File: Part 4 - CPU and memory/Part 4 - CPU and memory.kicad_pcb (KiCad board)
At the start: 2 copper layers, 100 x 100 mm, 50 parts, among them J1 BUS 1, U1 74AHC00, U10 SST39SF010, U11 AS6C4008, U2 74AHC32, U3 74AHC32, U4 74AHC32, U5 74HC563, U6 74AHC174, U7 74AHC138, U8 Z80C0010, U9 74HC563

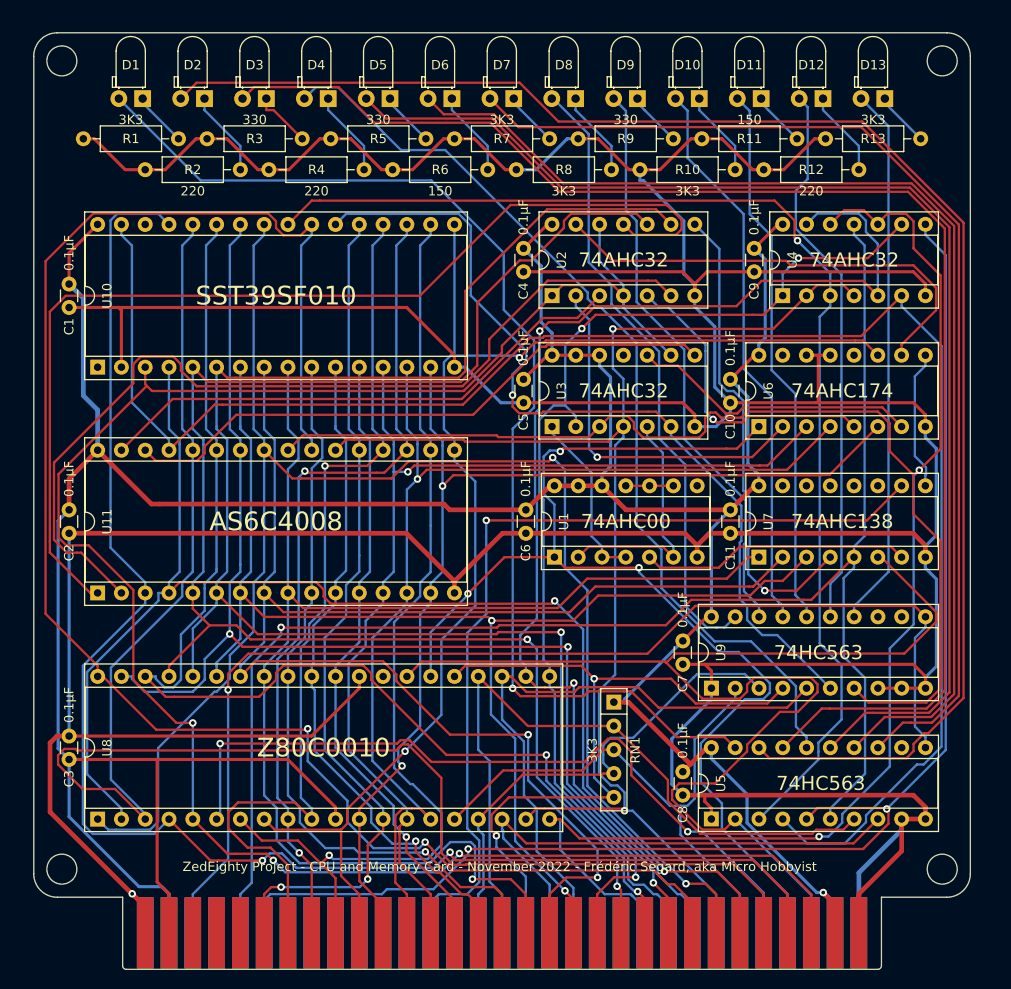
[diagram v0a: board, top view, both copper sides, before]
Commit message: Changed the clock for even cleaner clock switching
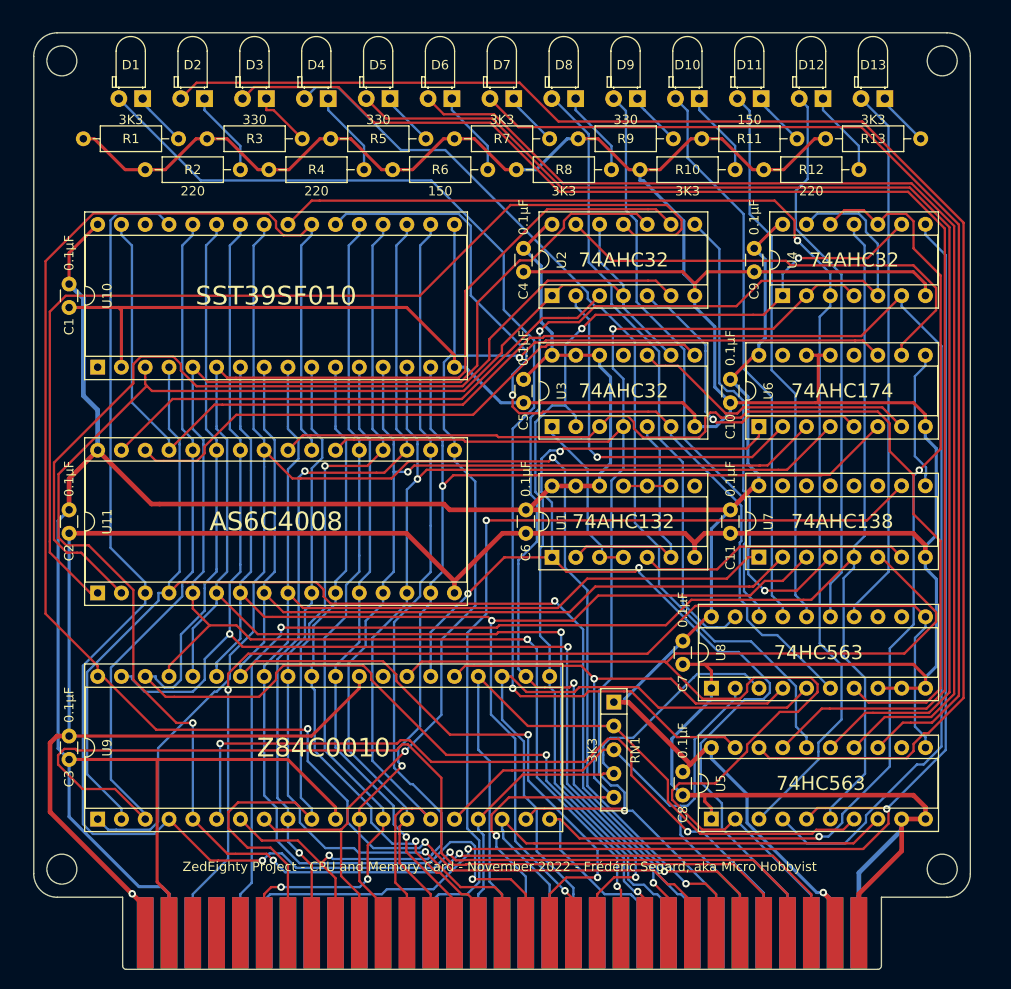
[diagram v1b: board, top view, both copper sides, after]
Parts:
- J1: value BUS 1 -> EDGE
- U1: value 74AHC00 -> 74AHC132
- U9: renamed from U8; value Z80C0010 -> Z84C0010
- moved U1 0.26 mm to (138.9, 96.5)
- renumbered U9 to U8
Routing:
- net +5V: track 359.5 -> 366.5 mm
- net /~{RESET}: track 120.5 -> 121.6 mm
- net /~{RD}: track 116.6 -> 117.3 mm
- net /~{WR}: track 130.7 -> 131.3 mm

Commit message: Added Keyboard, and minor fixes
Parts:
- removed the C9 at (160.5, 63.5)
- removed the U4 at (163.6, 68.6)
- D3: renamed from D2; value ~{MEMRD} -> ~{MEMRQ}
- D5: renamed from D3; value ~{MEMWR} -> ~{IORQ}
- D7: renamed from D4; value ~{IORD} -> ~{RD}
- D9: renamed from D5; value ~{IOWR} -> ~{WR}
- U1: value 74AHC132 -> 74AC00
- U2: renamed from U3; value 74AHC32 -> 74AC32
- U3: renamed from U7; value 74AHC138 -> 74AC138
- U7: renamed from U2; value 74AHC32 -> 74AC32
- U8: renamed from U6; value 74AHC174 -> 74AC174
- moved C7 41.9 mm to (153.2, 63.5)
- moved C8 41.9 mm to (153.2, 77.5)
- moved U10 41.9 mm to (156.2, 68.5)
- moved U9 41.9 mm to (156.2, 82.5)
- moved C10 28.0 mm to (158.3, 119.4)
- moved C9 28.0 mm to (158.3, 105.5)
- moved U3 28.0 mm to (161.3, 124.5)
- moved U8 28.0 mm to (161.3, 110.5)
- moved U1 24.9 mm to (163.8, 96.5)
- moved C6 24.6 mm to (160.8, 91.5)
- moved C4 17.6 mm to (143.7, 79.2), turned to 180 degrees
- moved C5 9.06 mm to (143.7, 82.0), turned to 180 degrees
- moved U7 7.62 mm to (138.7, 61.0), turned to 0 degrees
- moved U2 2.55 mm to (138.7, 85.1), turned to 0 degrees
- moved RN1 0.76 mm to (146.3, 112.0)
- renumbered C11 to C10, C10 to C9, D12 to D10, D6 to D11, D13 to D12, D7 to D13, D8 to D2, D9 to D4, D10 to D6, D11 to D8, R12 to R10, R6 to R11, R13 to R12, R7 to R13, R8 to R2, R2 to R3, R9 to R4, R3 to R5, R10 to R6, R4 to R7, R11 to R8, R5 to R9, U8 to U10, U9 to U4, U10 to U5, U11 to U6, U5 to U9
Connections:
- J1 pad 57: /~{IORD} -> /USER5
- J1 pad 58: /~{IOWR} -> /USER6
- RN1 pad 3: /~{INT} -> /~{BUSRQ}
- RN1 pad 4: /~{NMI} -> /~{INT}
- RN1 pad 5: /~{BUSRQ} -> /~{NMI}
- U2 pad 10: Net-(U3-Pad10) -> /~{WR}
- U2 pad 11: unconnected-(U3-Pad11) (its old number) -> Net-(U2-Pad11)
- U2 pad 12: +5V -> /A6
- U2 pad 13: +5V -> /A7
- U2 pad 8: /BA17 -> /~{IOWR}
- U2 pad 9: /A15 -> /~{IORQ}
- U3 pad 4: Net-(U2-Pad8) -> Net-(U2-Pad11)
- U5 pad 24: /~{MEMRD} -> /~{RD}
- U5 pad 31: /~{MEMWR} -> /~{WR}
- U6 pad 29: /~{MEMWR} -> /~{WR}
- U7 pad 10: /A7 -> Net-(U7-Pad10)
- U7 pad 8: Net-(U2-Pad8) -> /BA17
- U7 pad 9: /A6 -> /A15
- U8 pad 7: Net-(U3-Pad10) -> Net-(U7-Pad10)
- U9 pad 3: /~{MEMRD} -> /~{MREQ}
- U9 pad 4: /~{MEMWR} -> /~{IORQ}
- U9 pad 5: /~{IORD} -> /~{RD}
- U9 pad 6: /~{IOWR} -> /~{WR}
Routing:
- net /~{MEMWR}: track 183.9 -> 0.00 mm
- net /~{IORD}: track 150.6 -> 0.00 mm, vias 2 -> 0
- net /~{MEMRD}: track 126.6 -> 0.00 mm, vias 1 -> 0
- net /~{IOWR}: track 166.1 -> 57.5 mm, vias 1 -> 2
- net Net-(D3-Pad2): track 166.6 -> 73.3 mm
- net Net-(D5-Pad2): track 150.9 -> 69.3 mm
- net /~{WR}: track 131.3 -> 198.6 mm, vias 2 -> 1
- net Net-(D9-Pad2): track 132.8 -> 67.1 mm
- net Net-(U7-Pad10): track 0.00 -> 60.4 mm, vias 0 -> 1
- net Net-(D13-Pad2): track 116.9 -> 57.9 mm
- net /~{IORQ}: track 132.4 -> 76.1 mm, vias 2 -> 0
- net Net-(U2-Pad8): track 51.2 -> 0.00 mm, vias 1 -> 0
- net Net-(U2-Pad11): track 0.00 -> 49.9 mm, vias 0 -> 2
- net Net-(D11-Pad2): track 124.8 -> 75.7 mm
- net Net-(D1-Pad2): track 123.5 -> 77.4 mm, vias 1 -> 0
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- added copper zone on B.Cu, net GND
- added copper zone on F.Cu, net GND
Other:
- board text added: "74AC00"
- board text added: "74AC138"
- board text added: "74AC174"
- board text added: "74AC32"
- board text added: "74HC563"
- board text added: "AS6C4008"
- board text added: "SST39SF010"
- board text added: "Z84C0010"
- board text added: "ZedEighty Project - CPU and Memory Card - Rev 1 - Frédéric Segard - youtube.com/@microhobbyist"
- board text removed: "ZedEighty Project - CPU and Memory Card - November 2022 - Frédéric Segard, aka Micro Hobbyist"

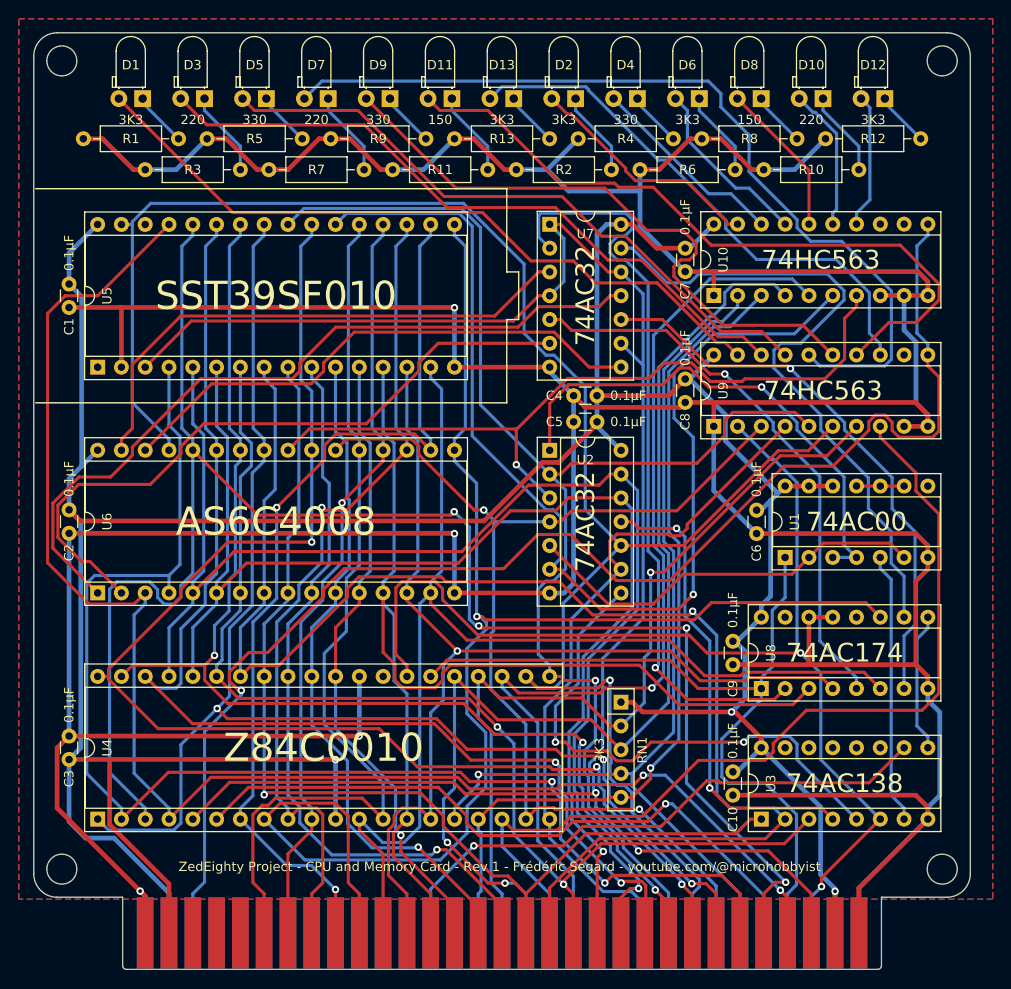
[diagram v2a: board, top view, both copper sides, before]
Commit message: Updated key library and keyboard
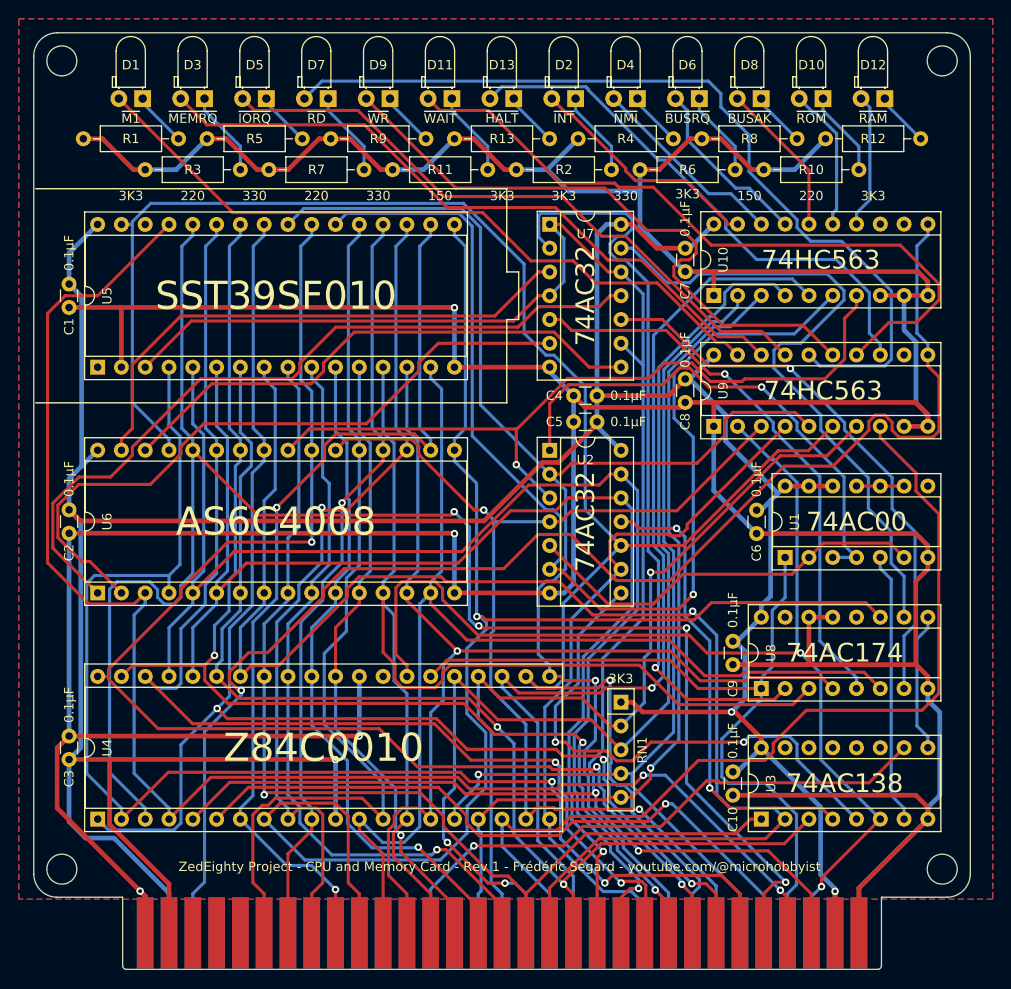
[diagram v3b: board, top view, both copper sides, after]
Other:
- rule pad_to_mask_clearance: 0 -> 0.2
- board text added: "150"
- board text added: "220"
- board text added: "330"
- board text added: "3K3"
- board text added: "~{BUSAK}"
- board text added: "~{BUSRQ}"
- board text added: "~{HALT}"
- board text added: "~{INT}"
- board text added: "~{IORQ}"
- board text added: "~{M1}"
- board text added: "~{MEMRQ}"
- board text added: "~{NMI}"
- board text added: "~{RAM}"
- board text added: "~{RD}"
- board text added: "~{ROM}"
- board text added: "~{WAIT}"
- board text added: "~{WR}"
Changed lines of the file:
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@@
       (dielectric_constraints no)
     )
-    (pad_to_mask_clearance 0)
+    (pad_to_mask_clearance 0.2)
+    (solder_mask_min_width 0.05)
     (pcbplotparams
       (layerselection 0x00010fc_ffffffff)
@@
       (psa4output false)
       (plotreference true)
-      (plotvalue false)
+      (plotvalue true)
       (plotinvisibletext false)
       (sketchpadsonfab false)
@@
       (effects (font (size 1 1) (thickness 0.15)))
     )
-    (fp_text value "330" (at 5.08 2.032) (layer "F.SilkS")
+    (fp_text value "330" (at 5.08 -6.096) (layer "F.SilkS")
       (effects (font (size 1 1) (thickness 0.15)))
     )
@@
       (effects (font (size 1 1) (thickness 0.15)))
     )
-    (fp_text value "220" (at 5.08 5.334) (layer "F.SilkS")
+    (fp_text value "220" (at 5.08 -2.794) (layer "F.SilkS")
       (effects (font (size 1 1) (thickness 0.15)))
     )
@@
       (effects (font (size 1 1) (thickness 0.15)))
     )
-    (fp_text value "0.1µF" (at -3.322 0 90) (layer "F.SilkS")
+    (fp_text value "0.1µF" (at -3.1242 0 90) (layer "F.SilkS")
       (effects (font (size 1 1) (thickness 0.15)))
     )
@@
       (effects (font (size 1 1) (thickness 0.15)))
     )
-    (fp_text value "330" (at 5.08 2.032) (layer "F.SilkS")
+    (fp_text value "330" (at 5.08 -6.096) (layer "F.SilkS")
       (effects (font (size 1 1) (thickness 0.15)))
     )
@@
       (effects (font (size 1 1) (thickness 0.15)))
     )
-    (fp_text value "220" (at 5.08 5.334) (layer "F.SilkS")
+    (fp_text value "220" (at 5.08 -2.794) (layer "F.SilkS")
       (effects (font (size 1 1) (thickness 0.15)))
     )
@@
       (effects (font (size 1 1) (thickness 0.15)))
     )
-    (fp_text value "3K3" (at 5.08 2.032) (layer "F.SilkS")
+    (fp_text value "3K3" (at 5.08 -6.096) (layer "F.SilkS")
       (effects (font (size 1 1) (thickness 0.15)))
     )
@@
       (effects (font (size 1 1) (thickness 0.15)))
     )
-    (fp_text value "3K3" (at 5.08 2.032) (layer "F.SilkS")
+    (fp_text value "3K3" (at 5.08 -6.096) (layer "F.SilkS")
       (effects (font (size 1 1) (thickness 0.15)))
     )
@@
       (effects (font (size 1 1) (thickness 0.15)))
     )
-    (fp_text value "150" (at 5.08 2.032) (layer "F.SilkS")
+    (fp_text value "150" (at 5.08 -6.096) (layer "F.SilkS")
       (effects (font (size 1 1) (thickness 0.15)))
     )
@@
       (effects (font (size 1 1) (thickness 0.15)))
     )
-    (fp_text value "3K3" (at 5.08 2.032) (layer "F.SilkS")
+    (fp_text value "3K3" (at 5.0546 -6.096) (layer "F.SilkS")
       (effects (font (size 1 1) (thickness 0.15)))
     )
@@
       (effects (font (size 1 1) (thickness 0.15)))
     )
-    (fp_text value "220" (at 5.08 5.334) (layer "F.SilkS")
+    (fp_text value "220" (at 5.08 -2.794) (layer "F.SilkS")
       (effects (font (size 1 1) (thickness 0.15)))
     )
@@
       (effects (font (size 1 1) (thickness 0.15)))
     )
-    (fp_text value "3K3" (at 5.08 5.334) (layer "F.SilkS")
+    (fp_text value "3K3" (at 5.08 -2.5908) (layer "F.SilkS")
       (effects (font (size 1 1) (thickness 0.15)))
     )
@@
       (effects (font (size 1 1) (thickness 0.15)))
     )
-    (fp_text value "330" (at 5.08 2.032) (layer "F.SilkS")
+    (fp_text value "330" (at 5.08 -6.096) (layer "F.SilkS")
       (effects (font (size 1 1) (thickness 0.15)))
     )
@@
       (effects (font (size 1 1) (thickness 0.15)))
     )
-    (fp_text value "0.1µF" (at -3.322 0 90) (layer "F.SilkS")
+    (fp_text value "0.1µF" (at -3.1496 0 90) (layer "F.SilkS")
       (effects (font (size 1 1) (thickness 0.15)))
     )
@@
       (effects (font (size 1 1) (thickness 0.15)))
     )
-    (fp_text value "150" (at 5.08 5.334) (layer "F.SilkS")
+    (fp_text value "150" (at 5.08 -2.794) (layer "F.SilkS")
       (effects (font (size 1 1) (thickness 0.15)))
     )
@@
       (effects (font (size 1 1) (thickness 0.15)))
     )
-    (fp_text value "3K3" (at 5.08 5.334) (layer "F.SilkS")
+    (fp_text value "3K3" (at 5.08 -2.794) (layer "F.SilkS")
       (effects (font (size 1 1) (thickness 0.15)))
     )
@@
       (effects (font (size 1 1) (thickness 0.15)))
     )
-    (fp_text value "3K3" (at 5.12 2.286 90) (layer "F.SilkS")
+    (fp_text value "3K3" (at -2.5 0 180) (layer "F.SilkS")
       (effects (font (size 1 1) (thickness 0.15)))
     )
@@
   (gr_line (start 90.17 68.585) (end 90.17 57.15) (layer "F.Fab") (width 0.1))
   (gr_line (start 128.524 60.96) (end 134.112 60.96) (layer "F.Fab") (width 0.1))
-  (gr_text "74AC32" (at 142.621 92.71 90) (layer "B.SilkS")
+  (gr_text "150" (at 127 55.118) (layer "B.SilkS")
+    (effects (font (size 1 1) (thickness 0.15)) (justify mirror))
+  )
+  (gr_text "3K3" (at 133.604 51.816) (layer "B.SilkS")
+    (effects (font (size 1 1) (thickness 0.15)) (justify mirror))
+  )
+  (gr_text "74AC32" (at 142.24 92.71 270) (layer "B.SilkS")
     (effects (font (size 2 2) (thickness 0.2)) (justify mirror))
   )
@@
     (effects (font (size 2 2) (thickness 0.2)) (justify mirror))
   )
+  (gr_text "220" (at 166.624 55.118) (layer "B.SilkS")
+    (effects (font (size 1 1) (thickness 0.15)) (justify mirror))
+  )
   (gr_text "AS6C4008" (at 109.474 92.71) (layer "B.SilkS")
     (effects (font (size 3 3) (thickness 0.2)) (justify mirror))
@@
     (effects (font (size 2 2) (thickness 0.2)) (justify mirror))
   )
+  (gr_text "330" (at 107.188 51.816) (layer "B.SilkS")
+    (effects (font (size 1 1) (thickness 0.15)) (justify mirror))
+  )
+  (gr_text "220" (at 113.792 55.118) (layer "B.SilkS")
+    (effects (font (size 1 1) (thickness 0.15)) (justify mirror))
+  )
+  (gr_text "3K3" (at 144.018 117.0559 90) (layer "B.SilkS")
+    (effects (font (size 1 1) (thickness 0.15)) (justify mirror))
+  )
   (gr_text "JLCJLCJLCJLC" (at 133.604 129.54) (layer "B.SilkS")
     (effects (font (size 1 1) (thickness 0.15)) (justify mirror))
   )
+  (gr_text "3K3" (at 93.98 51.816) (layer "B.SilkS")
+    (effects (font (size 1 1) (thickness 0.15)) (justify mirror))
+  )
+  (gr_text "3K3" (at 173.228 51.816) (layer "B.SilkS")
+    (effects (font (size 1 1) (thickness 0.15)) (justify mirror))
+  )
+  (gr_text "150" (at 160.02 51.816) (layer "B.SilkS")
+    (effects (font (size 1 1) (thickness 0.15)) (justify mirror))
+  )
+  (gr_text "220" (at 100.584 55.118) (layer "B.SilkS")
+    (effects (font (size 1 1) (thickness 0.15)) (justify mirror))
+  )
   (gr_text "74HC563" (at 167.64 64.643) (layer "B.SilkS")
     (effects (font (size 2 2) (thickness 0.2)) (justify mirror))
   )
+  (gr_text "3K3" (at 153.416 55.118) (layer "B.SilkS")
+    (effects (font (size 1 1) (thickness 0.15)) (justify mirror))
+  )
+  (gr_text "330" (at 146.812 51.816) (layer "B.SilkS")
+    (effects (font (size 1 1) (thickness 0.15)) (justify mirror))
+  )
+  (gr_text "330" (at 120.142 51.816) (layer "B.SilkS")
+    (effects (font (size 1 1) (thickness 0.15)) (justify mirror))
+  )
   (gr_text "SST39SF010" (at 109.474 68.58) (layer "B.SilkS")
     (effects (font (size 3 3) (thickness 0.2)) (justify mirror))
   )
+  (gr_text "3K3" (at 140.208 55.118) (layer "B.SilkS")
+    (effects (font (size 1 1) (thickness 0.15)) (justify mirror))
+  )
   (gr_text "74AC174" (at 170.18 106.68) (layer "B.SilkS")
     (effects (font (size 2 2) (thickness 0.2)) (justify mirror))
   )
-  (gr_text "74AC32" (at 142.494 68.707 90) (layer "B.SilkS")
+  (gr_text "74AC32" (at 142.24 68.707 270) (layer "B.SilkS")
     (effects (font (size 2 2) (thickness 0.2)) (justify mirror))
   )
+  (gr_text "~{BUSRQ}" (at 153.416 49.657) (layer "F.SilkS")
+    (effects (font (size 1 1) (thickness 0.15)))
+  )
+  (gr_text "~{HALT}" (at 133.604 49.63468) (layer "F.SilkS")
+    (effects (font (size 1 1) (thickness 0.15)))
+  )
+  (gr_text "~{IORQ}" (at 107.188 49.657) (layer "F.SilkS")
+    (effects (font (size 1 1) (thickness 0.15)))
+  )
+  (gr_text "~{MEMRQ}" (at 100.584 49.657) (layer "F.SilkS")
+    (effects (font (size 1 1) (thickness 0.15)))
+  )
+  (gr_text "~{ROM}" (at 166.624 49.657) (layer "F.SilkS")
+    (effects (font (size 1 1) (thickness 0.15)))
+  )
   (gr_text "ZedEighty Project - CPU and Memory Card - Rev 1 - Frédéric Segard - youtube.com/@microhobbyist" (at 133.35 129.54) (layer "F.SilkS")
     (effects (font (size 1 1) (thickness 0.15)))
   )
+  (gr_text "~{WAIT}" (at 127 49.657) (layer "F.SilkS")
+    (effects (font (size 1 1) (thickness 0.15)))
+  )
+  (gr_text "~{INT}" (at 140.208 49.657) (layer "F.SilkS")
+    (effects (font (size 1 1) (thickness 0.15)))
+  )
+  (gr_text "~{WR}" (at 120.396 49.657) (layer "F.SilkS")
+    (effects (font (size 1 1) (thickness 0.15)))
+  )
+  (gr_text "~{M1}" (at 93.98 49.657) (layer "F.SilkS")
+    (effects (font (size 1 1) (thickness 0.15)))
+  )
+  (gr_text "~{BUSAK}" (at 160.02 49.657) (layer "F.SilkS")
+    (effects (font (size 1 1) (thickness 0.15)))
+  )
+  (gr_text "~{NMI}" (at 146.812 49.657) (layer "F.SilkS")
+    (effects (font (size 1 1) (thickness 0.15)))
+  )
+  (gr_text "~{RAM}" (at 173.228 49.657) (layer "F.SilkS")
+    (effects (font (size 1 1) (thickness 0.15)))
+  )
+  (gr_text "~{RD}" (at 113.792 49.657) (layer "F.SilkS")
+    (effects (font (size 1 1) (thickness 0.15)))
+  )
